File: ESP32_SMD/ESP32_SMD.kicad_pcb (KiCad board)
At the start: 4 copper layers, 96.8 x 72.2 mm, 101 parts, among them J1 POWER(5V), J10 INPUT_2, J11 Conn_01x02_Socket, J12 Conn_01x02_Socket, J13 Conn_01x02_Socket, J14 Conn_01x02_Socket, J15 Conn_01x03_Socket, J16 Conn_01x15_Socket, J17 I2C, J18 Conn_01x03_Socket, J19 Conn_01x03_Socket, J2 Conn_01x02_Socket, J20 Conn_01x15_Socket, J21 Conn_01x02_Socket, J22 Conn_01x03_Socket, J23 Conn_01x03_Socket, J24 Conn_01x03_Socket, J25 POWER(3.3V), J3 FT234X, J4 I2C, J5 Conn_01x02_Socket, J6 Conn_01x02_Socket, J7 Conn_01x02_Socket, J8 Conn_01x02_Socket, J9 INPUT_1, SW1 SW_Nidec_CAS-120A1, SW2 BOOT, SW3 EN, U1 ESP32-WROOM-32E, U2 NJM2845DL1-33

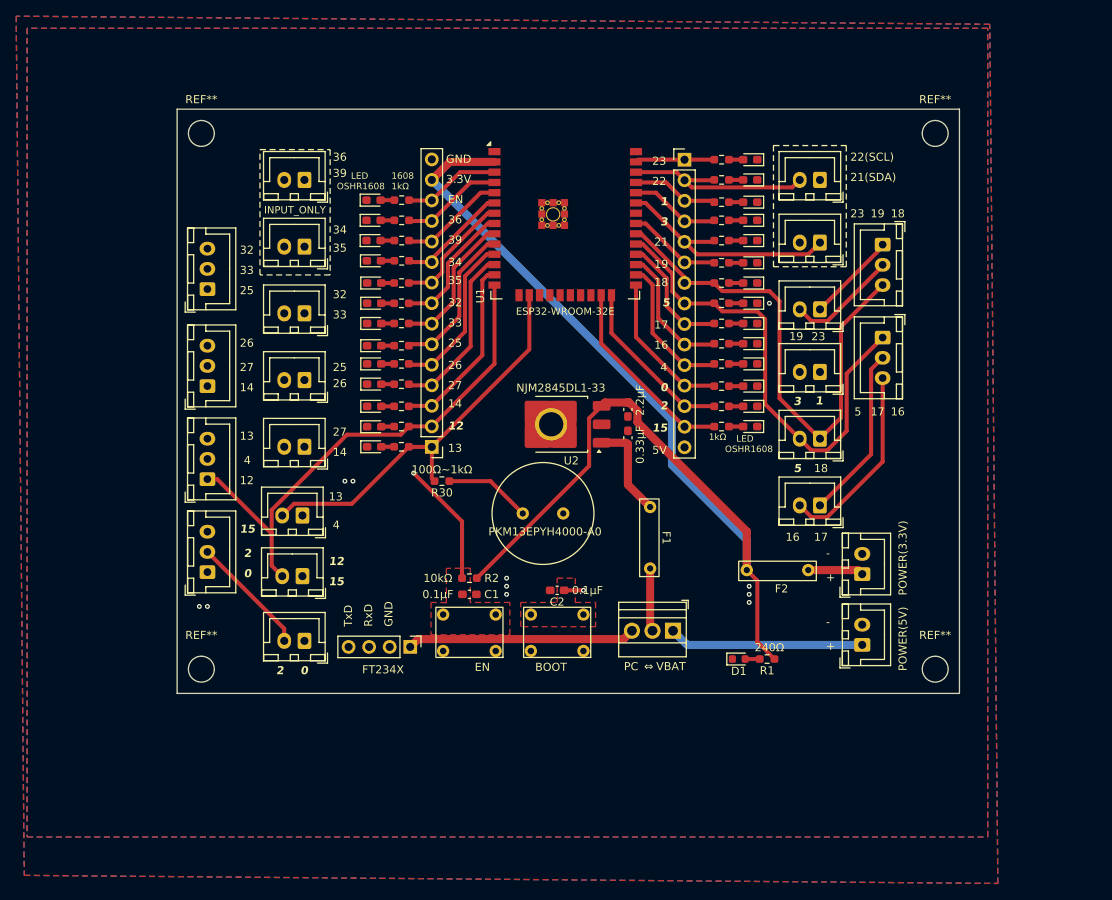
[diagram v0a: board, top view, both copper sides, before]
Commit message: USB-cポートとシリアル変換を乗せた
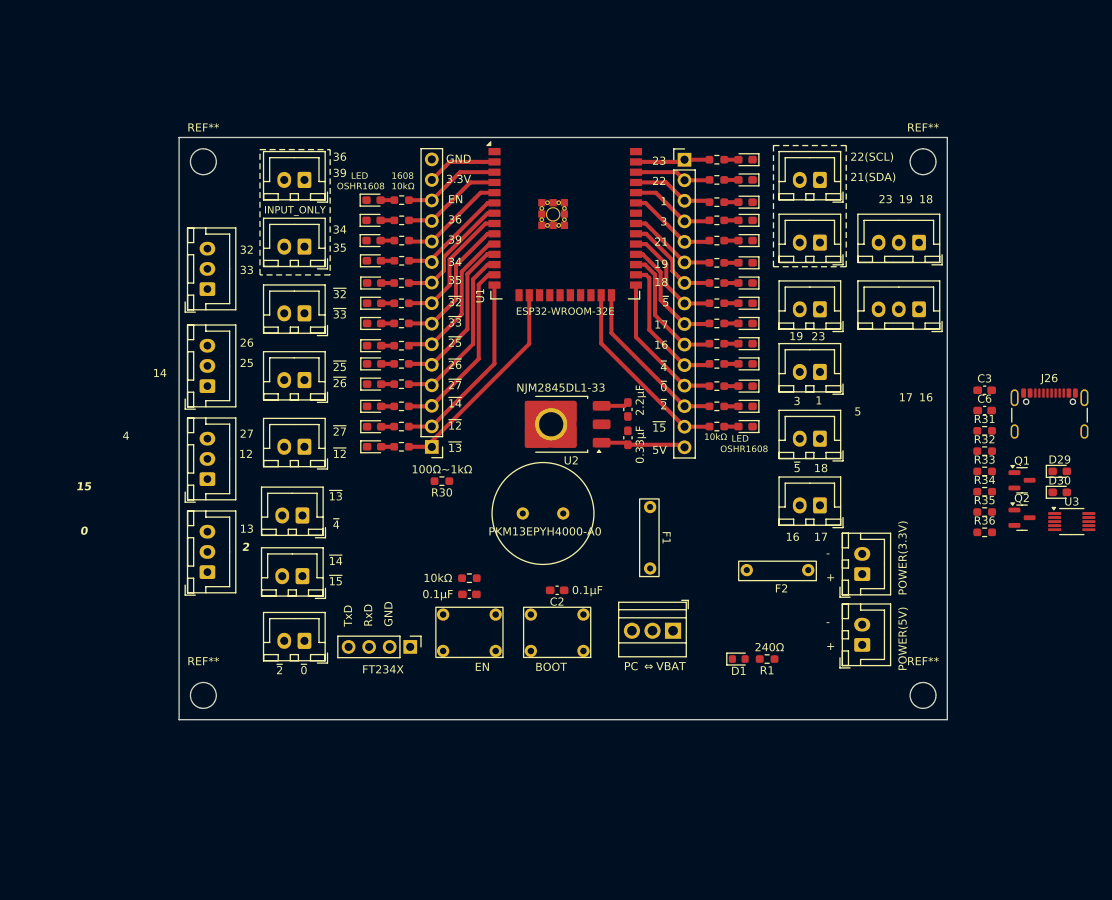
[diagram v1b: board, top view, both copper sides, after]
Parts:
- added C3: 0.1μF, Capacitor_SMD:C_0603_1608Metric_Pad1.08x0.95mm_HandSolder, F.Cu at (160.1, 80.3)
- added C6: 0.1μF, Capacitor_SMD:C_0603_1608Metric_Pad1.08x0.95mm_HandSolder, F.Cu at (160.1, 82.8)
- added D29: LED, LED_SMD:LED_0603_1608Metric_Pad1.05x0.95mm_HandSolder, F.Cu at (169.4, 90.3)
- added D30: LED, LED_SMD:LED_0603_1608Metric_Pad1.05x0.95mm_HandSolder, F.Cu at (169.4, 92.9)
- added J26: USB_C_Receptacle_USB2.0_16P, Connector_USB:USB_C_Receptacle_GCT_USB4105-xx-A_16P_TopMnt_Horizontal, F.Cu at (168.1, 84.3)
- added Q1: 2SC2712, Package_TO_SOT_SMD:SOT-23, F.Cu at (164.7, 91.4)
- added Q2: 2SC2712, Package_TO_SOT_SMD:SOT-23, F.Cu at (164.7, 96.0)
- added R31: 10kΩ, Resistor_SMD:R_0603_1608Metric_Pad0.98x0.95mm_HandSolder, F.Cu at (160.1, 85.3)
- added R32: 10kΩ, Resistor_SMD:R_0603_1608Metric_Pad0.98x0.95mm_HandSolder, F.Cu at (160.1, 87.8)
- added R33: 5.1kΩ, Resistor_SMD:R_0603_1608Metric_Pad0.98x0.95mm_HandSolder, F.Cu at (160.1, 90.3)
- added R34: 5.1kΩ, Resistor_SMD:R_0603_1608Metric_Pad0.98x0.95mm_HandSolder, F.Cu at (160.1, 92.8)
- added R35: 10kΩ, Resistor_SMD:R_0603_1608Metric_Pad0.98x0.95mm_HandSolder, F.Cu at (160.1, 95.3)
- added R36: 10kΩ, Resistor_SMD:R_0603_1608Metric_Pad0.98x0.95mm_HandSolder, F.Cu at (160.1, 97.8)
- added U3: CH340E, Package_SO:MSOP-10_3x3mm_P0.5mm, F.Cu at (170.9, 96.5)
- R10, R11, R12, R13, R14, R15, R16, R17, R18, R19, R20, R21, R22, R23, R24, R25, R26, R27, R28, R29, R3, R4, R5, R6, R7, R8, R9: value 1kΩ -> 10kΩ
- moved J18 5.70 mm to (152.0, 70.2), turned to 180 degrees
- moved J19 4.51 mm to (152.0, 62.0), turned to 180 degrees
- moved REF** 3.81 mm to (152.5, 52.0)
- moved REF** 3.58 mm to (152.5, 118.0)
- moved REF** 3.51 mm to (63.5, 52.0)
- moved REF** 3.26 mm to (63.5, 118.0)
- moved D2 0.59 mm to (130.5, 84.8)
- moved D21 0.59 mm to (130.5, 69.5)
- moved D22 0.59 mm to (130.5, 67.0)
- moved D23 0.59 mm to (130.5, 64.5)
- moved D24 0.59 mm to (130.5, 61.8)
- moved D25 0.59 mm to (130.5, 59.2)
- moved D26 0.59 mm to (130.5, 57.0)
- moved D27 0.59 mm to (130.5, 54.2)
- moved D28 0.59 mm to (130.5, 51.8)
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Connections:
- J11 pad 2: IO12 -> IO14
- J15 pad 1: IO25 -> GND
- J2 pad 1: TXD0/IO1 -> RXD0/IO3
- J20 pad 3: TXD0/IO1 -> RXD0/IO3
- J22 pad 1: IO14 -> GND
- J22 pad 2: IO27 -> IO25
- J23 pad 1: IO12 -> GND
- J23 pad 2: IO4 -> IO12
- J23 pad 3: IO13 -> IO27
- J24 pad 1: IO0 -> GND
- J24 pad 2: IO2 -> IO4
- J24 pad 3: IO15 -> IO13
- J3 pad 4: TXD0/IO1 -> RXD0/IO3
- J6 pad 1: IO14 -> IO12
- R27 pad 2: TXD0/IO1 -> RXD0/IO3
- U1 pad 35: TXD0/IO1 -> RXD0/IO3
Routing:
- net +3.3V: track 143.5 -> 12.1 mm
- net TXD0/IO1: track 114.2 -> 0.00 mm
- net RXD0/IO3: track 104.0 -> 20.7 mm
- net IO2: track 102.7 -> 20.6 mm
- net IO0: track 97.4 -> 18.0 mm, vias 1 -> 0
- net IO4: track 88.7 -> 17.5 mm
- net IO15: track 93.1 -> 23.6 mm
- net IO17: track 66.1 -> 14.7 mm
- net IO18: track 62.9 -> 12.4 mm
- net IO16: track 66.4 -> 16.2 mm
- net EN: track 62.2 -> 12.0 mm, vias 1 -> 0
- net IO5: track 58.5 -> 13.7 mm
- net IO12: track 64.2 -> 23.5 mm
- net IO23: track 46.4 -> 9.20 mm
- net IO13: track 63.5 -> 26.6 mm
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- removed copper zone on F.Cu, net EN
- removed copper zone on B.Cu, net GND
- removed copper zone on F.Cu, net GND
- removed copper zone on F.Cu, net IO0
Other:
- board size 96.8 x 72.2 mm -> 95 x 72 mm
- copper layers 4 -> 2
- board text added: "10kΩ"
- board text added: "1608 10kΩ"
- board text added: "~{0}"
- board text added: "~{12}"
- board text added: "~{13}"
- board text added: "~{14}"
- board text added: "~{15}"
- board text added: "~{25}"
- board text added: "~{26}"
- board text added: "~{27}"
- board text added: "~{2}"
- board text added: "~{32}"
- board text added: "~{33}"
- board text added: "~{4}"
- board text added: "~{5}"
- board text removed: "1608 1kΩ"
- board text removed: "1kΩ"

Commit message: 2.1.0
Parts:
- removed D29, D30: LED, LED_SMD:LED_0603_1608Metric_Pad1.05x0.95mm_HandSolder
- removed F2: MF-R050, 00a:MF-R050
- removed R31, R32: 10kΩ, Resistor_SMD:R_0603_1608Metric_Pad0.98x0.95mm_HandSolder
- added C7: 22μF, Capacitor_SMD:C_0603_1608Metric_Pad1.08x0.95mm_HandSolder, F.Cu at (127.4, 104.5)
- added C8: 100nF, Capacitor_SMD:C_0603_1608Metric_Pad1.08x0.95mm_HandSolder, F.Cu at (127.4, 102.2)
- added C9: 100nF, Capacitor_SMD:C_0603_1608Metric_Pad1.08x0.95mm_HandSolder, F.Cu at (138.6, 100.0)
- added J27: RJ45_Shielded, Connector_RJ:RJ45_Amphenol_RJHSE5380, F.Cu at (151.0, 100.8)
- added JP3: Jumper_2_Open, Connector_PinHeader_2.54mm:PinHeader_1x02_P2.54mm_Vertical, F.Cu at (136.2, 113.5)
- added JP4: Jumper_2_Open, Connector_PinHeader_2.54mm:PinHeader_1x02_P2.54mm_Vertical, F.Cu at (140.0, 111.0)
- added R37: 120Ω, Resistor_SMD:R_0603_1608Metric_Pad0.98x0.95mm_HandSolder, F.Cu at (138.4, 116.8)
- added U4: ATA6561, Package_SO:SOP-8_3.9x4.9mm_P1.27mm, F.Cu at (133.6, 103.4)
- J16, J20: footprint Connector_PinHeader_2.54mm:PinHeader_1x15_P2.54mm_Vertical -> Connector_PinSocket_2.54mm:PinSocket_1x15_P2.54mm_Vertical
- J25: value POWER(3.3V) -> RJ45_Shielded; footprint Connector_JST:JST_XH_B2B-XH-A_1x02_P2.50mm_Vertical -> Connector_RJ:RJ45_Amphenol_RJHSE5380
- R30: value 100Ω~1kΩ -> 240Ω
- moved Q2 79.6 mm to (85.8, 105.9), turned to 90 degrees
- moved R36 74.5 mm to (85.7, 102.1), turned to 90 degrees
- moved Q1 70.9 mm to (95.2, 105.7), turned to 90 degrees
- moved J26 66.6 mm to (110.0, 116.8)
- moved R35 65.2 mm to (95.2, 101.7), turned to 90 degrees
- moved U3 63.6 mm to (108.0, 105.9), turned to 90 degrees
- moved C3 58.8 mm to (105.4, 101.8)
- moved R33 58.7 mm to (104.8, 110.0), turned to 180 degrees
- moved C6 53.5 mm to (110.1, 101.8)
- moved R34 52.4 mm to (110.7, 110.0)
- moved R30 29.5 mm to (116.0, 73.0), turned to 0 degrees
- moved J3 29.0 mm to (113.3, 96.0)
- moved J1 26.0 mm to (119.2, 115.5), turned to 0 degrees
- moved J25 23.5 mm to (151.0, 80.2), turned to -90 degrees
- moved C2 22.4 mm to (85.6, 111.0)
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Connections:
- J13 pad 1: IO18 -> IO4
- J2 pad 1: RXD0/IO3 -> TXD0/IO1
- J20 pad 3: RXD0/IO3 -> TXD0/IO1
- J21 pad 1: IO0 -> IO18
- J21 pad 2: IO2 -> IO0
- J24 pad 2: IO4 -> IO2
- J25 pad 2: GND -> Net-(JP4-A)
- J3 pad 4: RXD0/IO3 -> TXD0/IO1
- J5 pad 1: IO4 -> IO2
- R27 pad 2: RXD0/IO3 -> TXD0/IO1
- R30 pad 2: IO13 -> IO0
- U1 pad 35: RXD0/IO3 -> TXD0/IO1
- U3 pad 9: RXD0/IO3 -> TXD0/IO1
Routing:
- net +3.3V: track 12.1 -> 145.5 mm, vias 0 -> 2
- net IO18: track 12.4 -> 111.1 mm, vias 0 -> 2
- net TXD0/IO1: track 0.00 -> 90.6 mm, vias 0 -> 5
- net IO5: track 13.7 -> 93.7 mm, vias 0 -> 1
- net IO0: track 18.0 -> 92.7 mm, vias 0 -> 1
- net EN: track 12.0 -> 78.8 mm, vias 0 -> 1
- net IO2: track 20.6 -> 84.8 mm, vias 0 -> 2
- net RXD0/IO3: track 20.7 -> 82.7 mm, vias 0 -> 5
- net IO17: track 14.7 -> 73.8 mm, vias 0 -> 1
- net IO16: track 16.2 -> 67.7 mm, vias 0 -> 1
- net IO15: track 23.6 -> 74.6 mm, vias 0 -> 2
- net Net-(JP3-B): track 0.00 -> 49.4 mm
- net IO4: track 17.5 -> 66.1 mm, vias 0 -> 1
- net IO23: track 9.20 -> 54.6 mm
- net Net-(JP4-A): track 0.00 -> 45.0 mm
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- added copper zone on B.Cu, net GND
- added copper zone on F.Cu, net GND
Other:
- board text added: "・右下のスイッチでPC給電と電源基盤給電 を変更できます。 ・I2Cは右上の破線部分に２つあります。 bootモードのやり方 ・BOOTボタンを押す(押しっぱなし) ・ENボタンを押す ・ENボタンを離す ・BOOTボタンを離す 2024/12/01 Yamamoto Maku"
- board text removed: "0"
- board text removed: "12"
- board text removed: "13"
- board text removed: "14"
- board text removed: "15"
- board text removed: "2"
- board text removed: "25"
- board text removed: "26"
- board text removed: "27"
- board text removed: "32"
- board text removed: "33"
- board text removed: "4"
- board text removed: "POWER(3.3V)"
- board text removed: "右下のスイッチでPC給電と電源基盤給電 を変更できます。 I2Cは右上の破線部分に２つあります。 bootモードのやり方 ・BOOTボタンを押す(押しっぱなし) ・ENボタンを押す ・ENボタンを離す ・BOOTボタンを離す 2024/11/05 Yamamoto Maku"

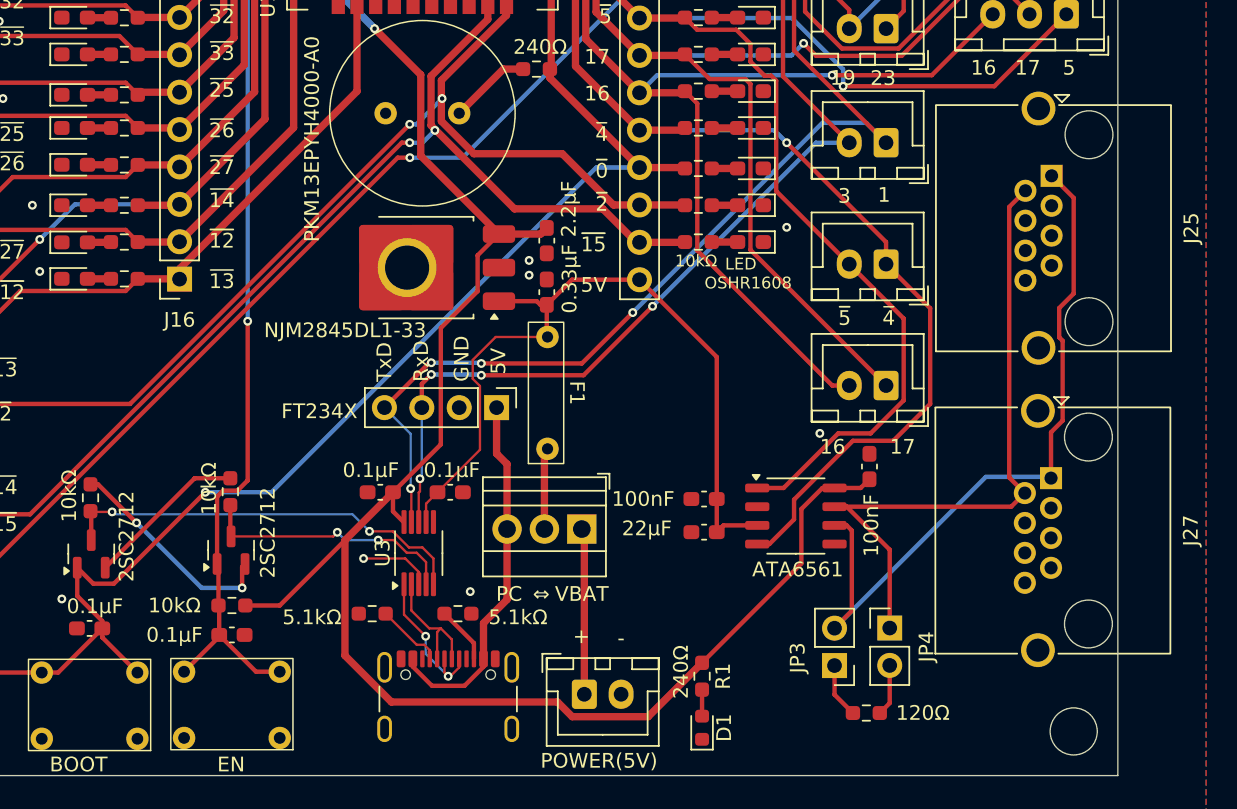
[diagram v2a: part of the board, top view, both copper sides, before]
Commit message: RJ45フットプリント修正,CH340E→CH340K
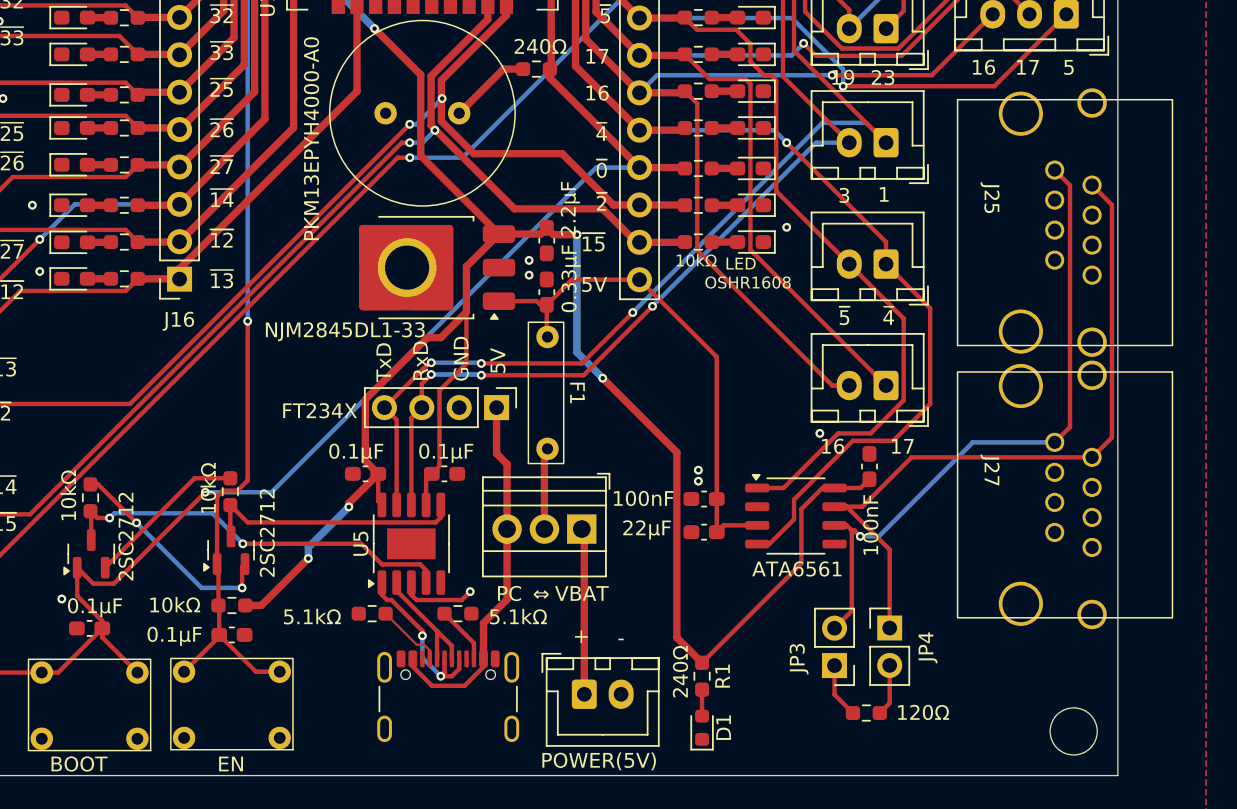
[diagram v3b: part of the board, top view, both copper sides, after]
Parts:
- removed U3: CH340E, Package_SO:MSOP-10_3x3mm_P0.5mm
- added U5: CH340K, Package_SO:SSOP-10-1EP_3.9x4.9mm_P1mm_EP2.1x3.3mm, F.Cu at (107.5, 105.2)
- J25, J27: footprint Connector_RJ:RJ45_Amphenol_RJHSE5380 -> 00a:RJ45
- moved J27 6.59 mm to (148.9, 94.5)
- moved J25 4.71 mm to (148.9, 76.0)
- moved C3 1.60 mm to (104.4, 100.5)
- moved C6 1.31 mm to (109.8, 100.5)
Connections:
- C6 pad 1: +5V -> +3.3V
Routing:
- net +5V: track 53.3 -> 34.8 mm
- net +3.3V: track 145.5 -> 155.1 mm, vias 2 -> 6
- net Net-(JP3-B): track 49.4 -> 44.4 mm, vias 0 -> 1
- net Net-(JP4-A): track 45.0 -> 48.8 mm
- net TXD0/IO1: track 90.6 -> 89.0 mm, vias 5 -> 4
- net Net-(U5-UD+): track 10.4 -> 11.6 mm
- net RXD0/IO3: track 82.7 -> 81.6 mm, vias 5 -> 4
- net Net-(Q2-E): track 28.4 -> 27.5 mm
- net GND: track 4.96 -> 5.22 mm, vias 18 -> 19
- net Net-(Q1-E): vias 2 -> 0
